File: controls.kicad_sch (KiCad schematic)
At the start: 23 parts, among them SW1 SW_DPST_x2, SW2 SW_DPST_x2, SW3 SW_DPST_x2, SW4 SW_DPST_x2, SW5 SW_DPST_x2, SW6 SW_DPST_x2, U1 ADG417BN, U2 ADG417BN, U3 ADG417BN, U4 ADG417BN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

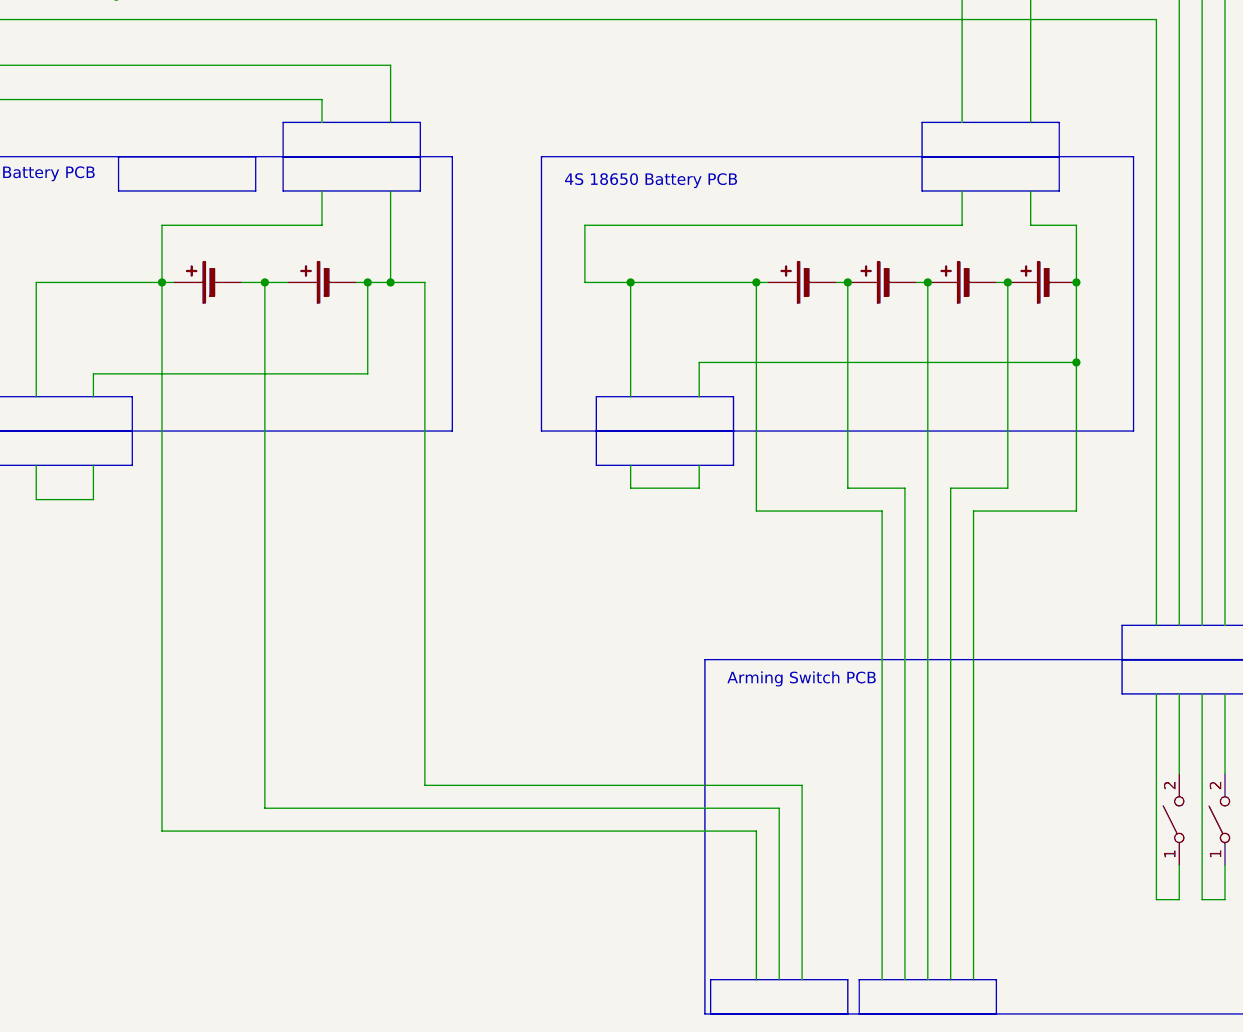
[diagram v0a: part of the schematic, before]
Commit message: Changed 4S to 2S2P
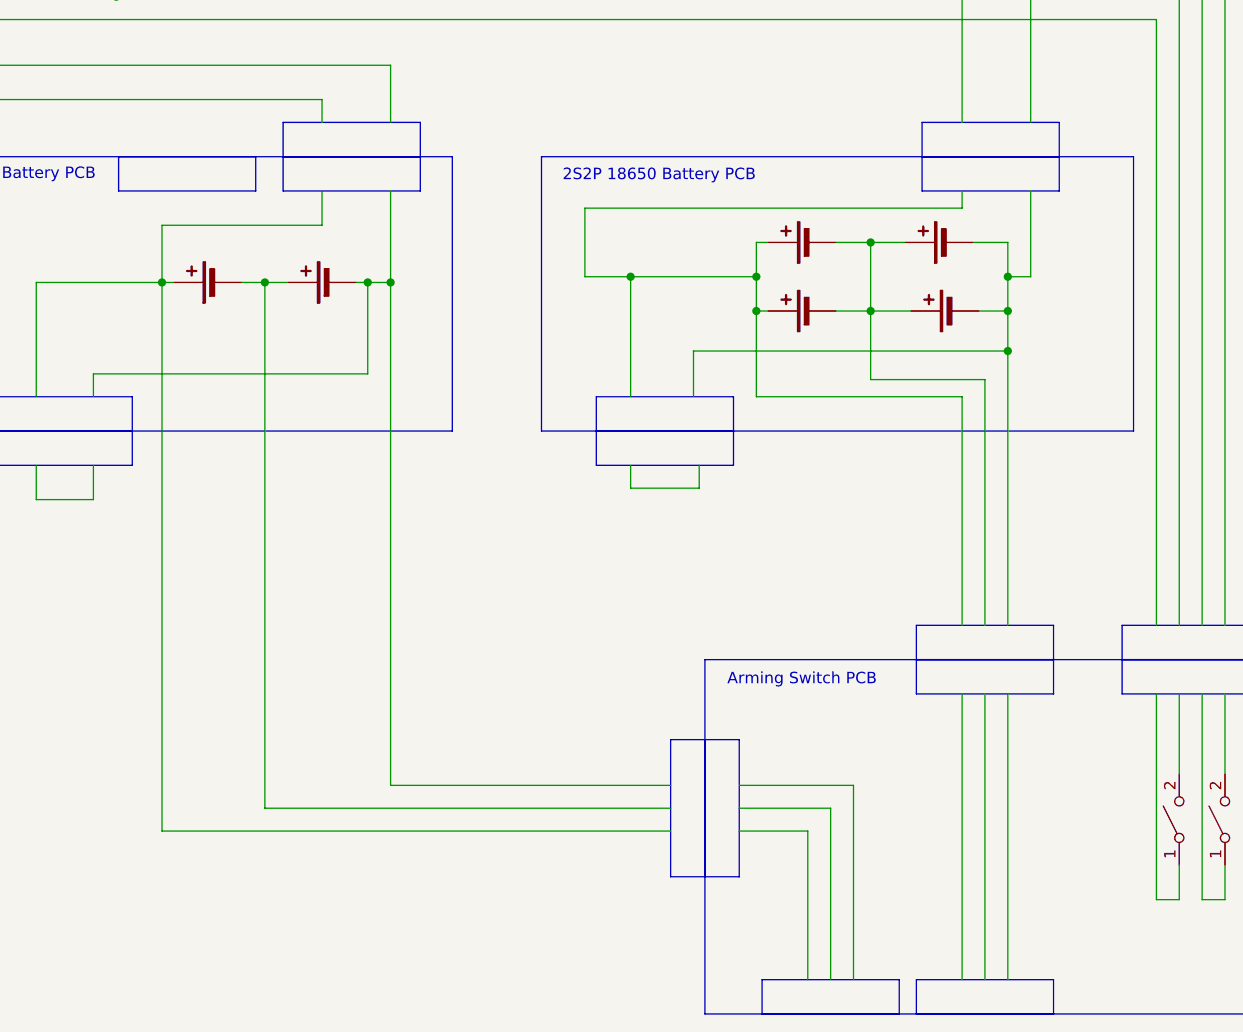
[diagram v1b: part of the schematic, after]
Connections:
- net at BT5.1 (+): now also BT3.1 (+); no longer BT4.2 (-)
- net at BT5.2 (-), BT6.1 (+): now also BT3.2 (-), BT4.1 (+)
- net at BT6.2 (-): now also BT4.2 (-)
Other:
- note added: "2S2P 18650 Battery PCB"
- note removed: "4S 18650 Battery PCB"

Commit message: update controls wiring diagram
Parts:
- removed BT3, BT4, BT5, BT6: Battery_Cell, symbol Device:Battery_Cell
- removed F1, F2, F3, F4, F5, F6: E-Match, symbol Device:Fuse
- removed SW1, SW2: SW_DPST_x2, symbol Switch:SW_DPST_x2
- removed U1, U2, U3, U4, U5: ADG417BN, Package_DIP:DIP-8_W7.62mm, symbol Analog_Switch:ADG417BN
- added BT10, BT7, BT8, BT9: Battery_Cell, symbol Device:Battery_Cell
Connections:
- new net: BT7.1 (+), BT9.1 (+)
- new net: BT10.1 (+), BT7.2 (-), BT8.1 (+), BT9.2 (-)
- new net: BT10.2 (-), BT8.2 (-)
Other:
- note added: "2S2P 18650 Battery Pack"
- note removed: "(Relays shown here are actually mosfets, they close the circuit when the control signal is low)"
- note removed: "2S2P 18650 Battery PCB"
- note removed: "A In: M1x2 1054301102"
- note removed: "A Out: S1x2"
- note removed: "Air Brake PCB"
- note removed: "Arming Switch: S1x2"
- note removed: "B In: M1x2 1054301102"
- note removed: "B Out: S1x2"
- note removed: "Battery: K1x2"
- note removed: "Battery: M1x2 1054301102"
- note removed: "Battery: S1x2"
- note removed: "Blue Raven"
- note removed: "C In: M1x2 1054301102"
- note removed: "C Out: S1x2"
- note removed: "CAN Termination PCB"
- note removed: "Camera PCB"
- note removed: "Drogue: S1x2"
- note removed: "E-Match Adapter Drogue Chute"
- note removed: "E-Match Adapter Main Chute"
- note removed: "E-Match: M2x3 1054051106"
- note removed: "Easy Mini"
- note removed: "Extension: M2x4 1054051108"
- note removed: "Featherweight GPS"
- note removed: "J1x2"
- note removed: "L1x2 534260210"
- note removed: "LR1x2 511630200"
- note removed: "M1x2 1054301102"
- note removed: "MCU STM32"
- note removed: "Main: S1x2"
- note removed: "Payload"
- note removed: "R1x2 1053071202"
- note removed: "R1x2 1053072202"
- note removed: "R2x2 1053081204"
- note removed: "R2x3 1053081206"
- note removed: "R2x4 1053051108"
- note removed: "Screw Terminal: S1x6"
- note removed: "Strain Gauges PCB 1"
- note removed: "Strain Gauges PCB 2"
- note removed: "Switches: M2x2 1054051104"
- note removed: "VL Mini"
- note removed: "Void Lake Fusion 4 (Equivalent Electrical Diagram) (Only Circuits Related to E-Matches are Shown)"
- company: (none) -> McMaster Rocketry Team
- title: (none) -> 2024-2025 Avionics Bay WIring Diagram

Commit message: reoriented drawing
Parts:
- added BT3, BT4, BT5: Battery_Cell, symbol Device:Battery_Cell
- added SW1: SW_DPST_x2, symbol Switch:SW_DPST_x2
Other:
- note added: "1S 18650 Battery Pack"
- note added: "2S 18650 Battery Pack"
- note added: "CAN BUS"
- note added: "CHARGING"
- note added: "POWER IN"
- note added: "POWER OUT"
- note removed: "1S 18650 Battery PCB"
- note removed: "2S 18650 Battery PCB"

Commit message: update cable colors
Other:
- note added: "Black: CAN Bus (Gray on wiring diagram)"
- note added: "Blue: Blue Raven Power"
- note added: "Gray: Featherweight GPS Power"
- note added: "Green: EasyMini Power"
- note added: "M1x2"
- note added: "M1x3"
- note added: "Orange: Shared 2S2P Power"
- note added: "Purple: Void Lake Power"
- note added: "WM1x2"
- title: 2024-2025 Avionics Bay WIring Diagram -> 2024-2025 Avionics Bay Wiring Diagram

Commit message: update controls diagram
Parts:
- removed SW6: SW_DPST_x2, symbol Switch:SW_DPST_x2
- added SW2: SW_DPST_x2, symbol Switch:SW_DPST_x2
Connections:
- net PWR: now reaches BT7.1 (+), BT9.1 (+)
- net PWR: now also BT2.1 (+), BT3.1 (+), BT4.1 (+), BT5.1 (+)
- net MID: now reaches BT10.1 (+), BT7.2 (-), BT8.1 (+), BT9.2 (-)
- net MID: now also BT1.1 (+), BT2.2 (-)
- net GND: now reaches BT5.2 (-)
- net GND: now also BT1.2 (-), BT10.2 (-), BT3.2 (-), BT4.2 (-), BT8.2 (-)
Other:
- note added: "Aero Rust"
- note added: "Air Brake PCB"
- note added: "Blue Raven"
- note added: "Bulkhead PCB"
- note added: "CAN Logger"
- note added: "Camera"
- note added: "EasyMini"
- note added: "Featherweight GPS"
- note added: "OZYS V3 #1"
- note added: "OZYS V3 #2"
- note added: "OZYS V3 #3"
- note added: "Recovery Beacon"
- note added: "VL Mini"
- note added: "VLFX"
- note removed: "CAN BUS"
- note removed: "M1x2"
- note removed: "M1x3"
- note removed: "POWER IN"
- note removed: "POWER OUT"
- note removed: "WM1x2"

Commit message: controls wiring diagram
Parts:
- removed BT1, BT2, BT7, BT9: Battery_Cell, symbol Device:Battery_Cell
- removed SW1, SW2, SW3, SW4, SW5: SW_DPST_x2, symbol Switch:SW_DPST_x2
- added BT11, BT12, BT17, BT6: Battery_Cell, symbol Device:Battery_Cell
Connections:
- net GND: now also BT12.2 (-), BT6.2 (-); no longer BT8.2 (-)
- net MID: now also BT8.2 (-), BT11.2 (-), BT12.1 (+), BT17.2 (-), BT6.1 (+); no longer BT8.1 (+)
- net PWR: now also BT8.1 (+), BT11.1 (+), BT17.1 (+)
- no-connect marks 0 -> 1
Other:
- note added: "A.M.P."
- note added: "BR_BAT"
- note added: "BR_PWR"
- note added: "BR_PYRO_DROG"
- note added: "BR_PYRO_MAIN"
- note added: "EM_BAT"
- note added: "EM_PWR"
- note added: "EM_PYRO_DROG"
- note added: "EM_PYRO_MAIN"
- note added: "FW_BAT"
- note added: "FW_PWR"
- note added: "FeatherWeight GPS"
- note added: "ICARUS"
- note added: "Payload Activation"
- note added: "SHARED_BAT"
- note added: "SHARED_PWR_1"
- note added: "SHARED_PWR_2"
- note added: "SHARED_PWR_3"
- note added: "SHARED_PWR_4"
- note added: "VL_BAT"
- note added: "VL_PWR"
- note added: "VL_PYRO_DROG"
- note added: "VL_PYRO_MAIN"
- note removed: "Air Brake PCB"
- note removed: "Arming Switch PCB"
- note removed: "CAN Logger"
- note removed: "CHARGING"
- note removed: "Featherweight GPS"
- note removed: "OZYS V3 #3"
- note removed: "Power Distribution PCB"

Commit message: controls wiring diagram
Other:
- note added: "VLF5"
